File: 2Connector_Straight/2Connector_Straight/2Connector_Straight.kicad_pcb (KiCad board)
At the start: 2 copper layers, 53.3 x 57.1 mm, 6 parts, among them J1 North_Temps_1, J2 North_Temps_2, J3 Internal_Temps_DCT_HSK_Box_1, J4 Internal_Temps_DCT_HSK_Box_2

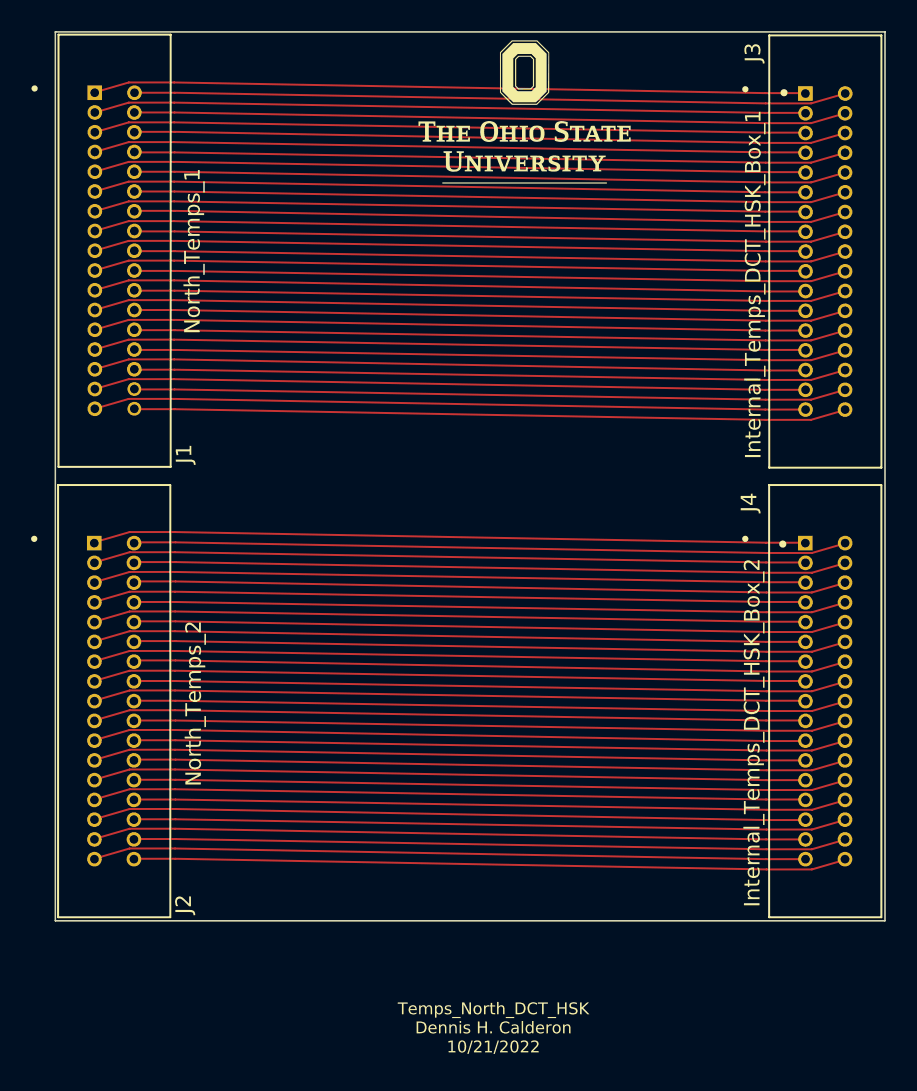
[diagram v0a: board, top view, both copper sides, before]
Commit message: Added little 2 connectyor to 2 connector board.
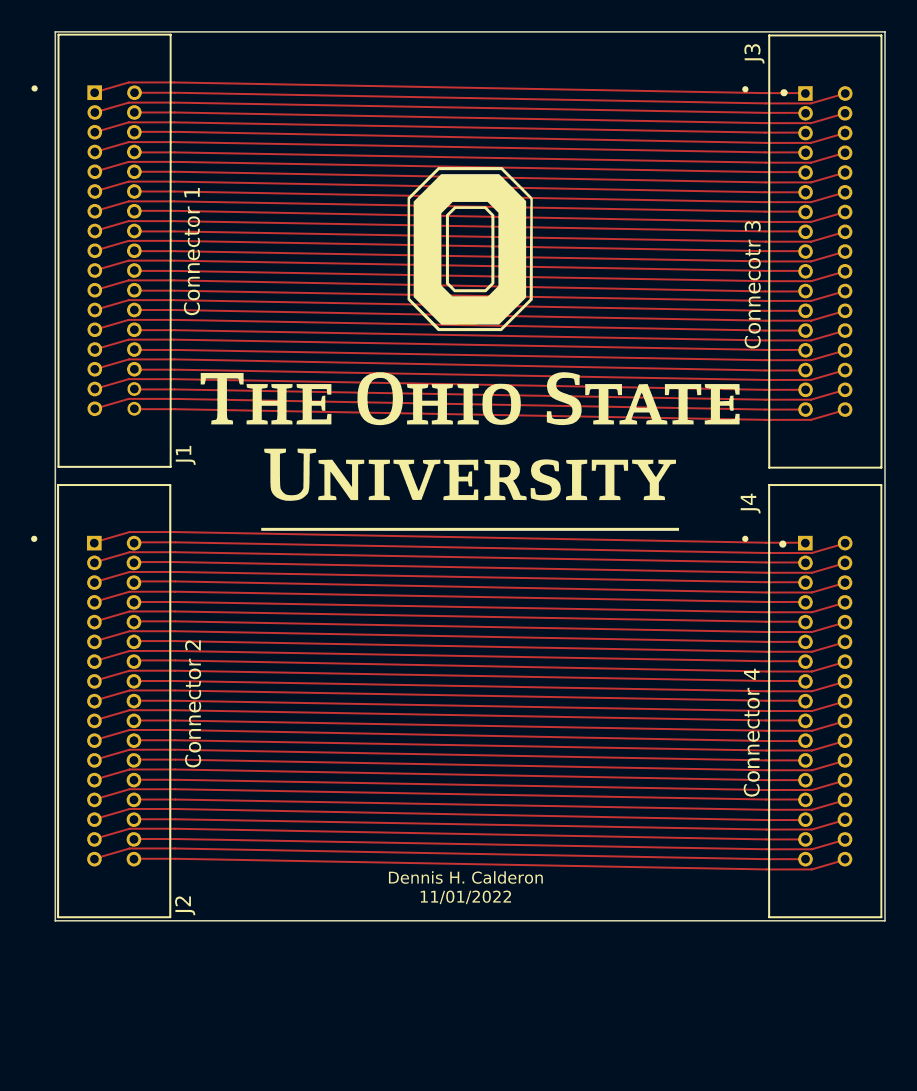
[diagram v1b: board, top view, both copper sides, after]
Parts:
- removed the G*** at (121.6, 52.1)
- added G***: LOGO, LOGO, F.Cu at (118.1, 67.4)
- added G***: LOGO, LOGO, B.Cu at (117.6, 71.3)
- J1: value North_Temps_1 -> Connector 1
- J2: value North_Temps_2 -> Connector 2
- J3: value Internal_Temps_DCT_HSK_Box_1 -> Connecotr 3
- J4: value Internal_Temps_DCT_HSK_Box_2 -> Connector 4
- moved G*** 21.4 mm to (118.1, 96.3), turned to 180 degrees
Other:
- board text added: "Dennis H. Calderon 11/01/2022"
- board text removed: "Temps_North_DCT_HSK Dennis H. Calderon 10/21/2022"
